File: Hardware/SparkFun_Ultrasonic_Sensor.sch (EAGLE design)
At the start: 50 parts, among them J2 BM04B-SRSS-TB, J3 BM04B-SRSS-TB, Q1 847, U2 STM8L051, U3 TCT40-16T, U4 TCT40-16R, U6 LMV324

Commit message: Removes almost any lingering parts from old design. Gets close to finishing schematic
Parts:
- removed ADDR_RST: (no value), Connector:TEST_POINT35MIL
- removed C10, C17, C7, C8, C9: 1uF ±10% 50V, Discretex:C-0603
- removed C4, C5: 100nF ±10% 50V, Discretex:C-0603
- removed J1: (no value), Connector:HEADER-4P-60/35MIL
- removed J3: BM04B-SRSS-TB, Connector:JST-SH-4P
- removed JP2: SMT-JUMPER_3_2-NC_TRACE, NOA-Jumpers:SMT-JUMPER_3_2-NC_TRACE
- removed R10: 100K ±1%, Discretex:R-0603
- removed R19, R21: 10k, SparkFun-Resistors:10KOHM-0603-1/10W-1%
- removed U1: (no value), IC:LMV324
- removed U2: STM8L051, IC:STM8L051
- removed U3: TCT40-16T, Discretex:TCT40-16T/R
- removed U4: TCT40-16R, Discretex:TCT40-16T/R
- added C18, C24, C25, C26, C27, C28, C6: 0.1uF, SparkFun-Capacitors:0.1UF-0603-25V-(+80/-20%)
- added FD1, FD2, FD3, FD4: FIDUCIAL1X2, SparkFun-Aesthetics:FIDUCIAL1X2
- added FRAME1: FRAME-LEDGER, SparkFun-Aesthetics:FRAME-LEDGER
- added H1, H2: STAND-OFFTIGHT, SparkFun-Hardware:STAND-OFFTIGHT
- added I2C: JUMPER-SMT_3_2-NC_TRACE_SILK, SparkFun-Jumpers:JUMPER-SMT_3_2-NC_TRACE_SILK
- added J4, J6: Vertical Qwiic Connector, SparkFun-Connectors:QWIIC_CONNECTOR
- added R11, R20: 10k, SparkFun-Resistors:10KOHM-0603-1/10W-1%
- added R24: 100k, SparkFun-Resistors:100KOHM-0603-1/10W-1%
- added TP1: TEST-POINT3X5, SparkFun-Connectors:TEST-POINT3X5
- added U7: STM8L051F3, new_parts:STM8L051F3
- added U8: SP3232EB, new_parts:SP3232EB
- added U9: ULTRASONIC_SENSOR_RECEIVER, new_parts:ULTRASONIC_SENSOR_RECEIVER
- C1, C14: value 10nF ±10% 50V -> 10nF; device Discretex:C-0603 -> SparkFun-Capacitors:10NF-0603-50V-10%
- C11, C13, C16, C3: value 1nF ±10% 50V -> 1nF; device Discretex:C-0603 -> SparkFun-Capacitors:1.0NF/1000PF-0603-50V-10%
- C12: value 68pF ±10% 50V -> 68pF; device Discretex:C-0603 -> SparkFun-Capacitors:68PF-0603-50V-5%
- C15: value 1uF ±10% 50V -> 1.0uF; device Discretex:C-0603 -> SparkFun-Capacitors:1.0UF-0603-16V-10%
- C2: value 1uF ±1% 50V -> 1.0uF; device Discretex:C-0603 -> SparkFun-Capacitors:1.0UF-0603-16V-10%
- J2: value BM04B-SRSS-TB -> (none); device Connector:JST-SH-4P -> SparkFun-Connectors:CONN_041X04_NO_SILK_NO_POP
- Q1: value 847 -> 600mA/40V; device Discrete:TRANSISTOR-NPN-SOT23'' -> SparkFun-DiscreteSemi:TRANS_NPN-MMBT2222AL
- R3: value 4.3K ±1% -> 4.3k; device Discretex:R-0603 -> SparkFun-Resistors:4.3KOHM-0402
- R4, R9: value 120K ±1% -> 124k; device Discretex:R-0603 -> SparkFun-Resistors:124KOHM
- R7: value 3.3M ±1% -> 2.2M; device Discretex:R-0603 -> SparkFun-Resistors:2.2MOHMS-0603-1/10W-1%
- R8: value 1K ±1% -> 1k; device Discretex:R-0603 -> SparkFun-Resistors:1KOHM-0603-1/10W-1%
- U5: value (none) -> ULTRASONIC_SENSOR_TRANSMITTER; device IC:UT3232G-S16-RSOIC-16 -> new_parts:ULTRASONIC_SENSOR_TRANSMITTER
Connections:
- removed net N$11: C15.2, C16.2, R12.1, R14.1, R18.1, R9.1, U1OP2.IN+, U1OP3.IN+, U1OP4.IN+
- removed net N$13: C7.1, U5.C1-
- removed net N$17: C8.2, U5.C2+
- removed net N$18: C8.1, U5.C2-
- removed net N$22: C9.2, U5.V+
- removed net N$23: C17.2, U5.V-
- removed net N$24: U3.-, U5.DOUT1
- removed net N$25: U3.+, U5.DOUT2
- removed net N$27: ADDR_RST.1, U2.PB5
- removed net N$28: R10.1, U2.PB4
- removed net N$42: U2.PA2
- removed net N$43: U2.PA3
- removed net N$44: U2.PC6
- removed net N$45: U2.PC5
- removed net N$7: C7.2, U5.C1+
- new net 3.3V: C2.2, C28.1, C6.1, I2C.2, J2.1, J4.2, J6.2, R11.2, R12.2, R8.2, U6G5.P$V+, U7.VCC/VREF+, U8.VCC
- new net ADDR_RST: TP1.1, U7.PB5
- new net N: R24.2, U7.PB4
- new net N$31: C15.2, C16.2, R12.1, R14.1, R18.1, R9.1, U6G2.+IN, U6G3.+IN, U6G4.+IN
- new net N$37: C25.2, U8.C1-
- new net N$38: C24.1, U8.C2+
- new net N$39: C24.2, U8.C2-
- new net N$40: C27.1, U8.V-
- new net N$41: C26.1, U8.V+
- new net N$48: U5.1, U8.T1OUT
- new net N$49: U5.2, U8.T2OUT
- new net N$8: C25.1, U8.C1+
- net +3V3: no longer C10.2, C2.2, C5.1, C9.1, J1.P$1, J2.VCC, J3.VCC, JP2.2, R12.2, R19.2, R8.2, U1OP1.V+, U2.VCC/VREF+, U5.VCC
- net DIN1: now also U7.PB1, U8.T1IN; no longer U2.PB0, U5.DIN1
- net DIN2: now also U7.PD0, U8.T2IN; no longer U2.PD0, U5.DIN2
- net ECHO: now also J2.3, U7.PB2; no longer J1.P$3, U2.PB2
- net GND: now also C18.2, C26.2, C27.2, C28.2, C6.2, J2.4, J4.1, J6.1, R20.1, U6G5.P$V-, U7.VSS/VREF-, U8.GND, U9.2; no longer C10.1, C17.1, C4.1, C5.2, J1.P$4, J2.5, J2.6, J2.GND, J3.5, J3.6, J3.GND, R21.2, U1OP1.V-, U2.GND/VREF-, U4.-, U5.GND
- net INT: now also U7.PB6; no longer U2.PB6
- net N$1: now also U6G3.OUT; no longer U1OP3.OUT
- net N$10: now also U6G2.OUT; no longer U1OP2.OUT
- net N$14: now also U6G4.OUT; no longer U1OP4.OUT
- net N$15: now also U6G4.-IN; no longer U1OP4.IN-
- net N$19: now also I2C.3; no longer JP2.3
- net N$2: now also U6G3.-IN; no longer U1OP3.IN-
- net N$20: now also I2C.1; no longer JP2.1
- net N$26: now also U9.1; no longer U4.+
- net N$4: now also U6G1.+IN; no longer U1OP1.IN+
- net N$6: now also U6G1.OUT; no longer U1OP1.OUT
- net N$9: now also U6G2.-IN; no longer U1OP2.IN-
- net NRST: now also C18.1, R11.1, U7.PA1/!RST!; no longer C4.2, R19.1, U2.NRST
- net PB4: now also R24.1, U6G1.-IN; no longer R10.2, U1OP1.IN-
- net SCL: now also J4.4, J6.4, U7.PC1; no longer J2.SCL, J3.SCL, U2.PC1
- net SDA: now also J4.3, J6.3, U7.PC0; no longer J2.SDA, J3.SDA, U2.PC0
- net SWIM: now also U7.PA0; no longer U2.PA0
- net TRIG: now also J2.2, R20.2, U7.PB3; no longer J1.P$2, R21.1, U2.PB3
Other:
- note added: "Revised By: Elias Santistevan"
- moved on the sheet: R1, R12, R13, R14, R15, R16, R17, R18, R22, R23, R5, R6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

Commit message: Finishes up schematic
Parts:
- removed J5: (no value), Connector:HEADER-4P-TEST_3.08_4P
- added TP2, TP3, TP4, TP5, TP6: TEST-POINT3X5, SparkFun-Connectors:TEST-POINT3X5
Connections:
- removed net +3V3: J5.P$4
- net GND: no longer J5.P$1
- net INT: now also TP6.1
- net NRST: now also TP3.1; no longer J5.P$2
- net SCL: now also TP5.1
- net SDA: now also TP4.1
- net SWIM: now also TP2.1; no longer J5.P$3
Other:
- note added: "Header"
- note added: "Microcontroller - STM8L051F3"
- note added: "OP-AMP - LMV324 Ultrasonic Receiver - CUSA-R80"
- note added: "Qwiic Conncectors"
- note added: "RS-232 Transceiver - SP3232EB Ultrasonic Transmitter - CUSA-T80"
- note added: "Testpoints"
- note removed: "Qwiic Connector"
- note removed: "STM8"
- note removed: "SWIM"
- note removed: "Ultrasound reception"
- note removed: "Ultrasound transmission"
- moved on the sheet: C1, C11, C12, C13, C14, C15, C16, C18, C2, C24, C25, C26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

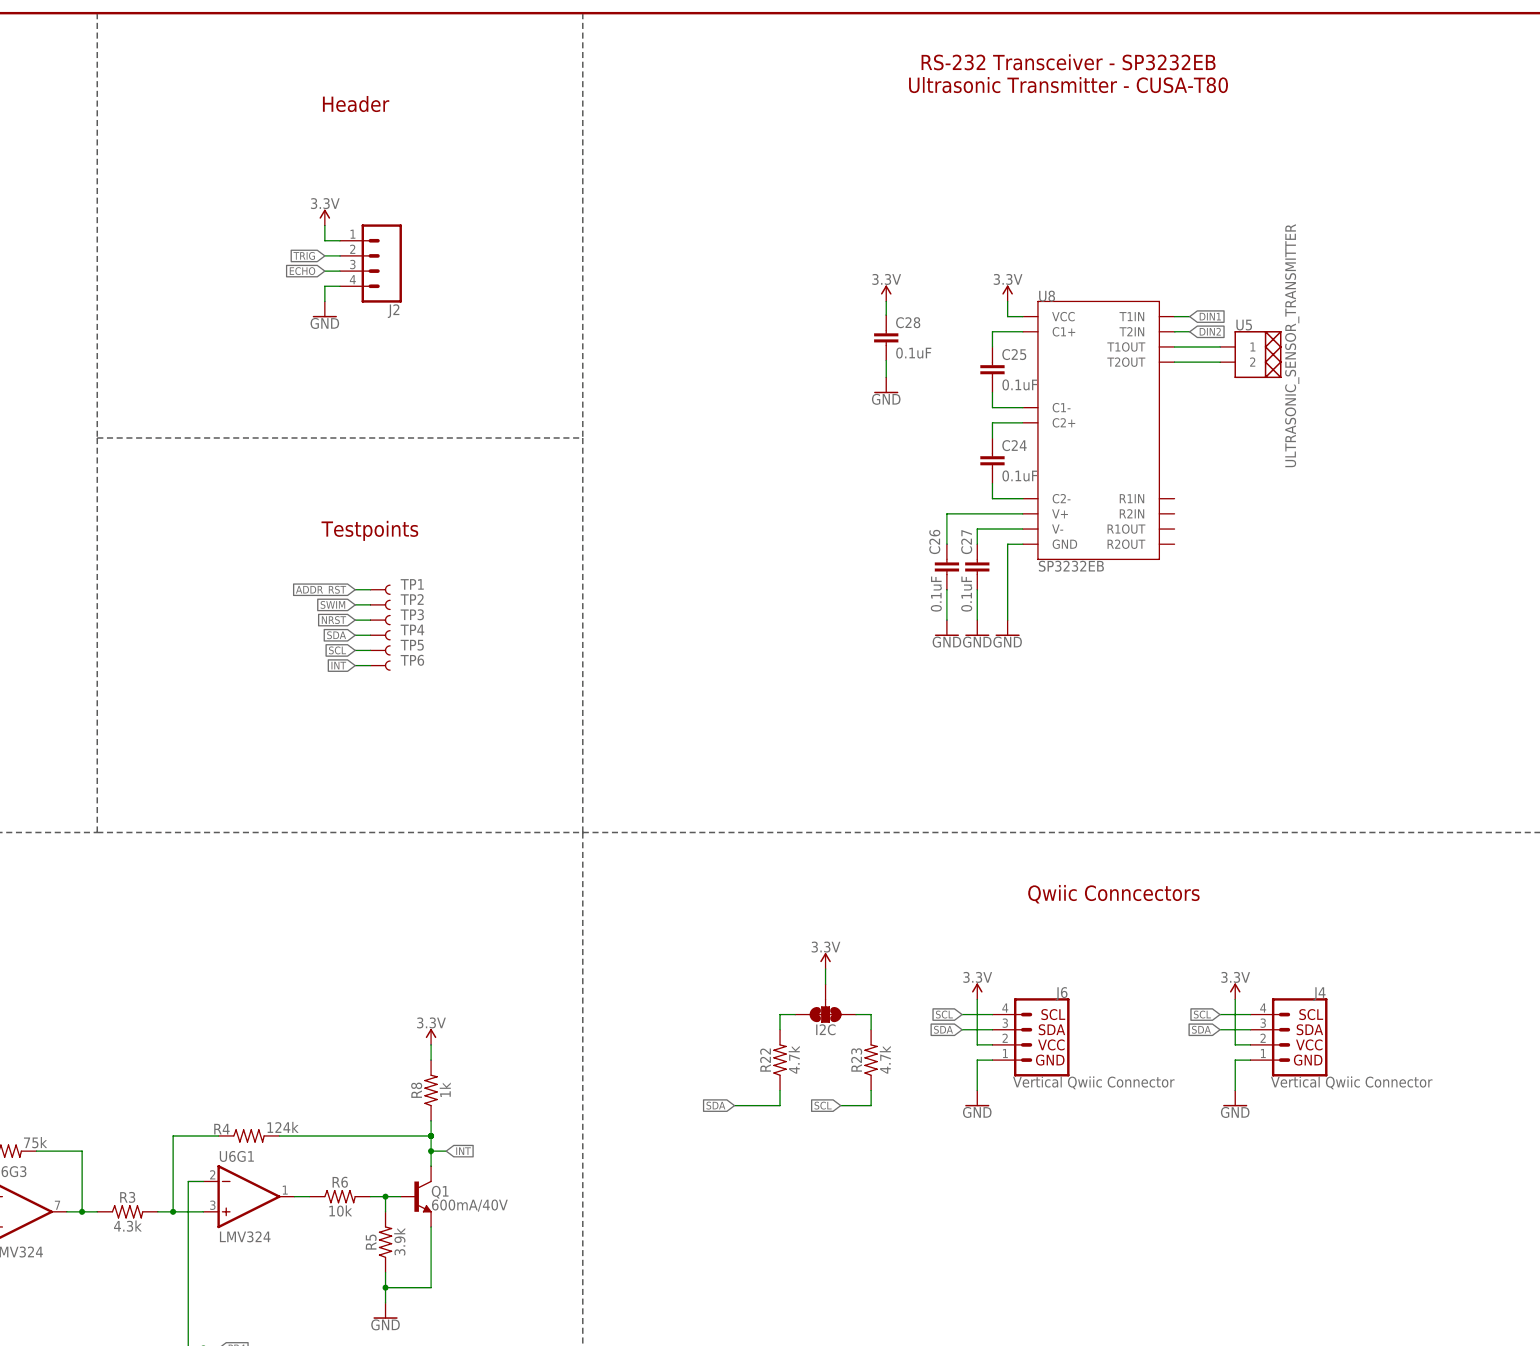
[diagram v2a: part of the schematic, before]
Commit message: Moves passives around the PCB
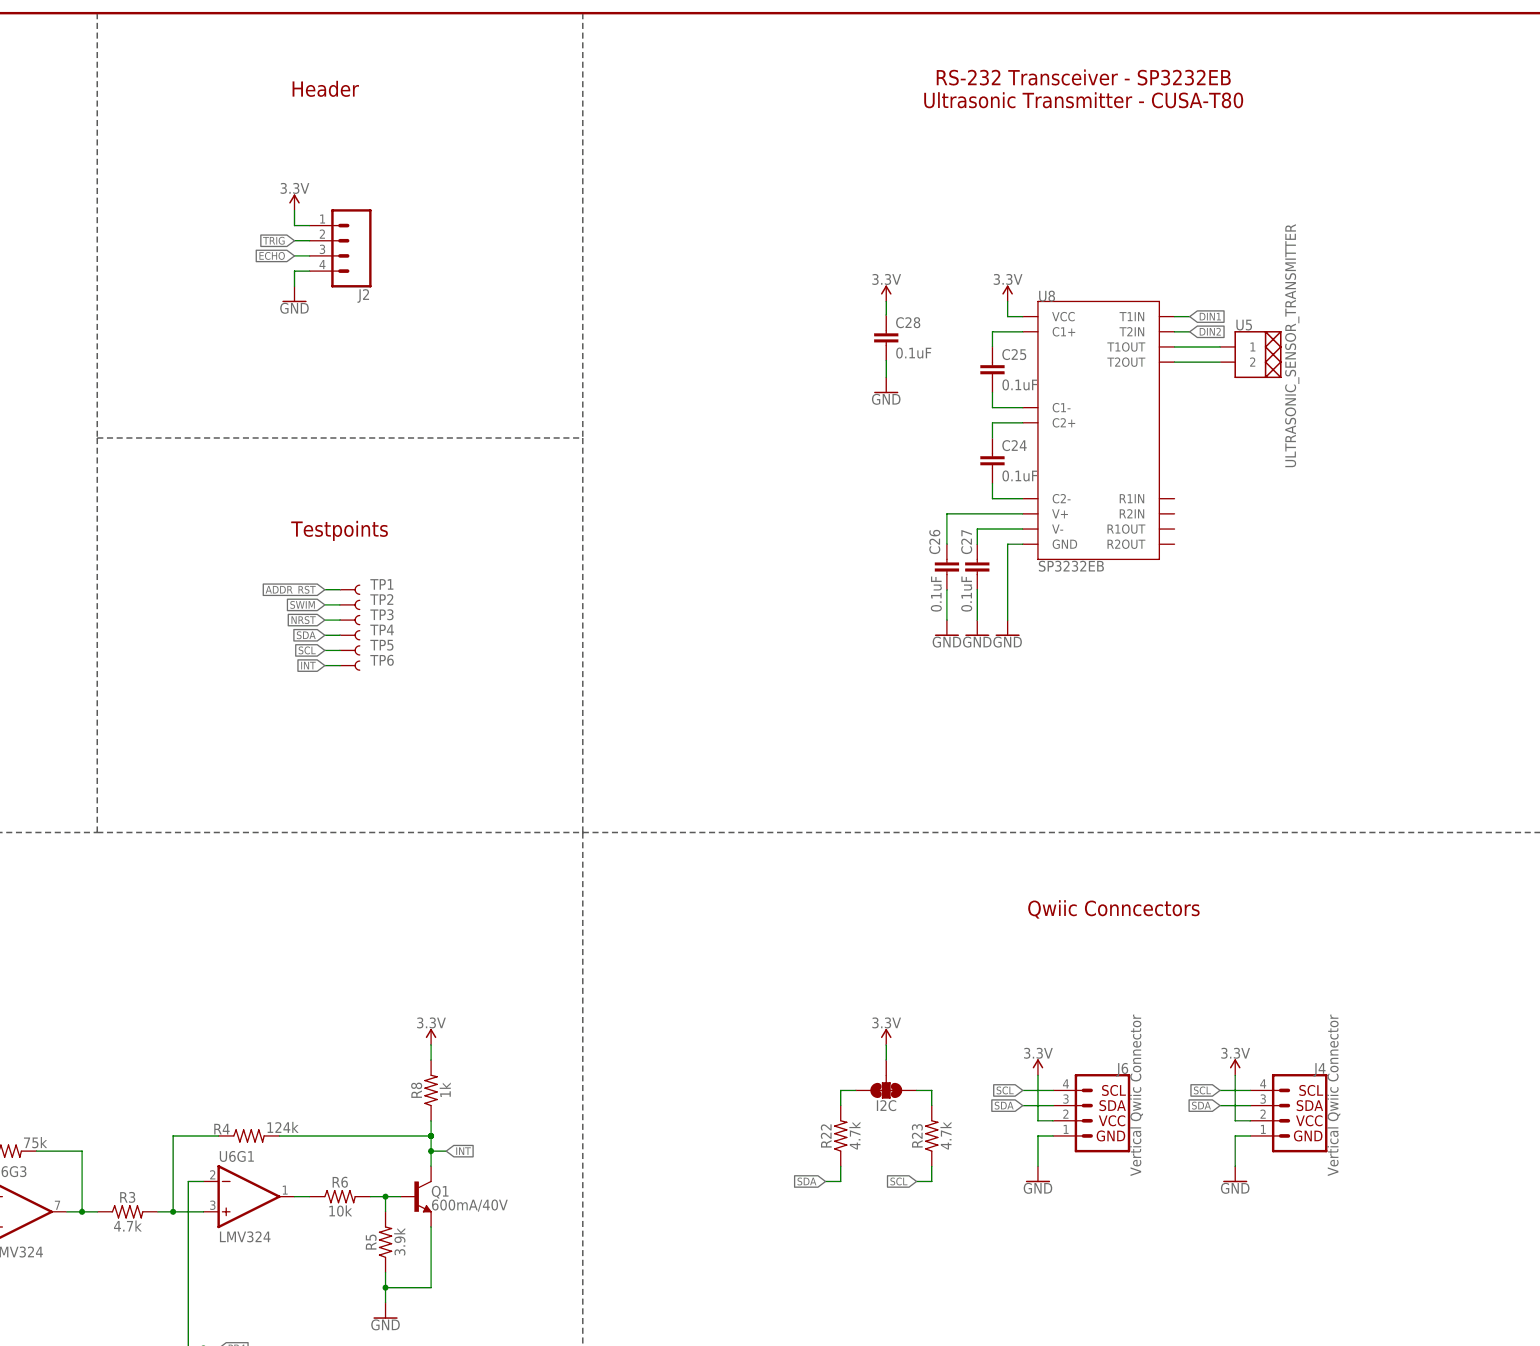
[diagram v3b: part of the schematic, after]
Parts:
- R3: value 4.3k -> 4.7k; device SparkFun-Resistors:4.3KOHM-0402 -> SparkFun-Resistors:4.7KOHM-0603-1/10W-1%
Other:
- moved on the sheet: I2C, J2, J4, J6, R22, R23, TP1, TP2, TP3, TP4, TP5, TP6

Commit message: Routes more wires
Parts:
- TP1, TP2, TP3, TP4, TP5, TP6: value TEST-POINT3X5 -> TEST-POINT3X4; device SparkFun-Connectors:TEST-POINT3X5 -> SparkFun-Connectors:TEST-POINT3X4
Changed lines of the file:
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@@
 <part name="GND17" library="SparkFun-PowerSymbols" deviceset="GND" device=""/>
 <part name="GND18" library="SparkFun-PowerSymbols" deviceset="GND" device=""/>
-<part name="TP1" library="SparkFun-Connectors" deviceset="TEST-POINT" device="3X5"/>
+<part name="TP1" library="SparkFun-Connectors" deviceset="TEST-POINT" device="3X4" value="TEST-POINT3X4"/>
 <part name="U8" library="new_parts" deviceset="SP3232EB" device=""/>
 <part name="FRAME1" library="SparkFun-Aesthetics" deviceset="FRAME-LEDGER" device="">
@@
 <part name="GND4" library="SparkFun-PowerSymbols" deviceset="GND" device=""/>
 <part name="J2" library="SparkFun-Connectors" deviceset="CONN_04" device="1X04_NO_SILK_NO_POP"/>
-<part name="TP2" library="SparkFun-Connectors" deviceset="TEST-POINT" device="3X5"/>
-<part name="TP3" library="SparkFun-Connectors" deviceset="TEST-POINT" device="3X5"/>
-<part name="TP4" library="SparkFun-Connectors" deviceset="TEST-POINT" device="3X5"/>
-<part name="TP5" library="SparkFun-Connectors" deviceset="TEST-POINT" device="3X5"/>
-<part name="TP6" library="SparkFun-Connectors" deviceset="TEST-POINT" device="3X5"/>
+<part name="TP2" library="SparkFun-Connectors" deviceset="TEST-POINT" device="3X4" value="TEST-POINT3X4"/>
+<part name="TP3" library="SparkFun-Connectors" deviceset="TEST-POINT" device="3X4" value="TEST-POINT3X4"/>
+<part name="TP4" library="SparkFun-Connectors" deviceset="TEST-POINT" device="3X4" value="TEST-POINT3X4"/>
+<part name="TP5" library="SparkFun-Connectors" deviceset="TEST-POINT" device="3X4" value="TEST-POINT3X4"/>
+<part name="TP6" library="SparkFun-Connectors" deviceset="TEST-POINT" device="3X4" value="TEST-POINT3X4"/>
 </parts>
 <sheets>

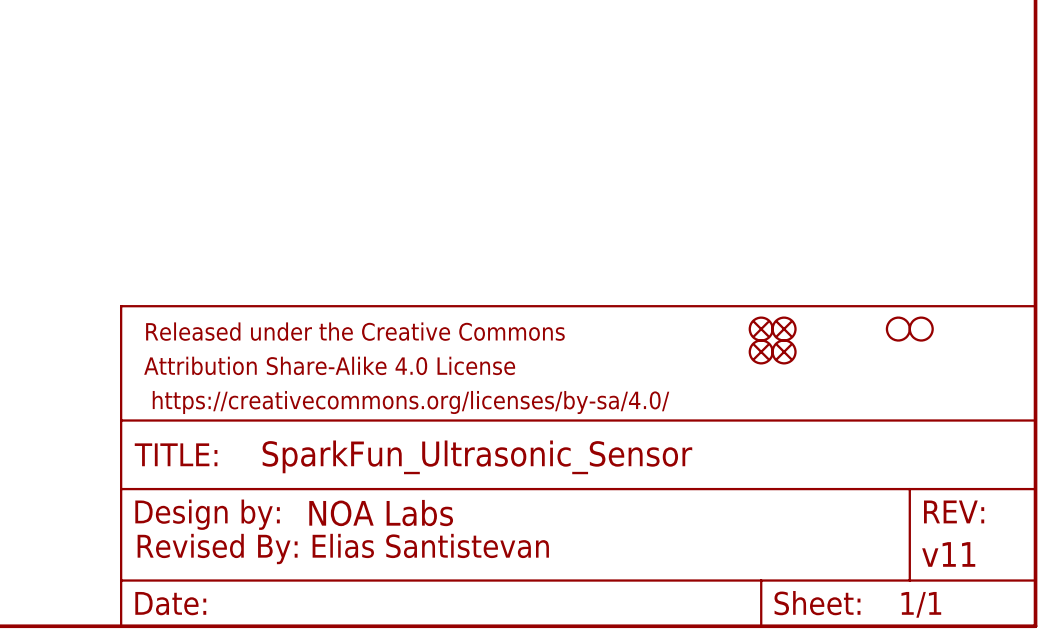
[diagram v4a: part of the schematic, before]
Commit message: Adds silk
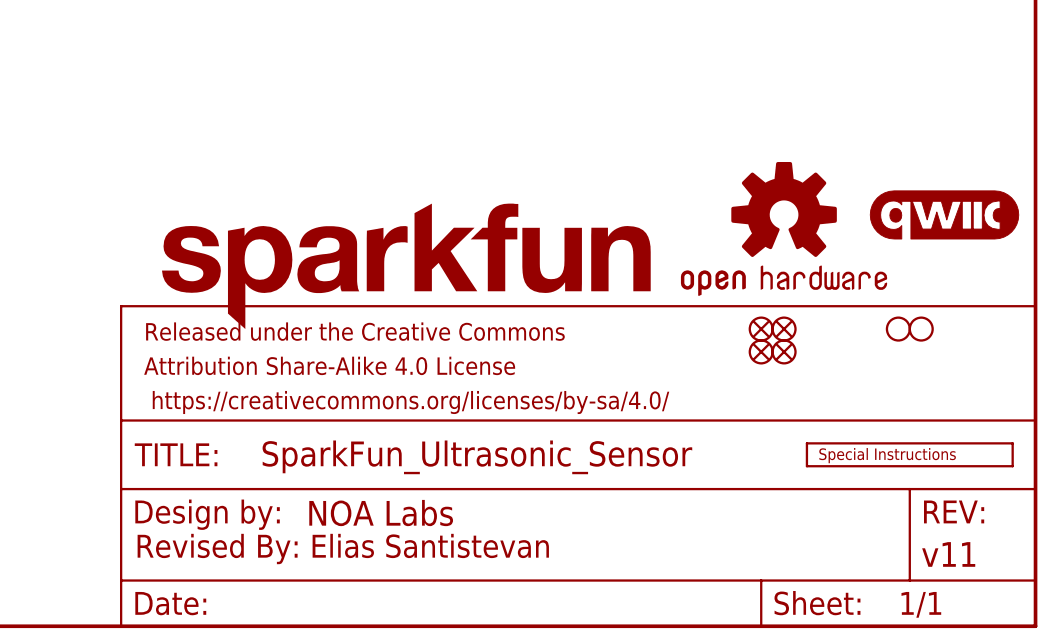
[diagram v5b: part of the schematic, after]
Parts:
- added LOGO1: SPECIAL_INSTRUCTIONS-ORDERING, SparkFun-Aesthetics:SPECIAL_INSTRUCTIONS-ORDERING
- added LOGO2: SFE_LOGO_NAME.1_INCH, SparkFun-Aesthetics:SFE_LOGO_NAME.1_INCH
- added LOGO3: QWIIC_LOGO_3MM, SparkFun-Aesthetics:QWIIC_LOGO_3MM
- added LOGO4: OSHW-LOGOS, SparkFun-Aesthetics:OSHW-LOGOS
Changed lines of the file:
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@@
 <part name="TP5" library="SparkFun-Connectors" deviceset="TEST-POINT" device="3X4" value="TEST-POINT3X4"/>
 <part name="TP6" library="SparkFun-Connectors" deviceset="TEST-POINT" device="3X4" value="TEST-POINT3X4"/>
+<part name="LOGO1" library="SparkFun-Aesthetics" deviceset="SPECIAL_INSTRUCTIONS" device="-ORDERING"/>
+<part name="LOGO2" library="SparkFun-Aesthetics" deviceset="SFE_LOGO_NAME" device=".1_INCH"/>
+<part name="LOGO3" library="SparkFun-Aesthetics" deviceset="QWIIC_LOGO" device="_3MM"/>
+<part name="LOGO4" library="SparkFun-Aesthetics" deviceset="OSHW-LOGO" device="S"/>
 </parts>
 <sheets>
@@
 <attribute name="NAME" x="223.52" y="170.18" size="1.778" layer="95" font="vector"/>
 </instance>
+<instance part="LOGO1" gate="G$1" x="406.4" y="17.78" smashed="yes"/>
+<instance part="LOGO2" gate="G$1" x="332.74" y="33.02" smashed="yes"/>
+<instance part="LOGO3" gate="G$1" x="421.64" y="45.72" smashed="yes"/>
+<instance part="LOGO4" gate="G$1" x="403.86" y="45.72" smashed="yes"/>
 </instances>
 <busses>
